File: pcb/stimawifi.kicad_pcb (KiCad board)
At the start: 2 copper layers, 62.9 x 48.8 mm, 12 parts, among them J1 Screw_Terminal_01x05, J2 Screw_Terminal_01x05, J3 Screw_Terminal_01x05, J4 Screw_Terminal_01x05, J5 Screw_Terminal_01x05, J8 Conn_01x02, U1 WEMOS_D1_mini

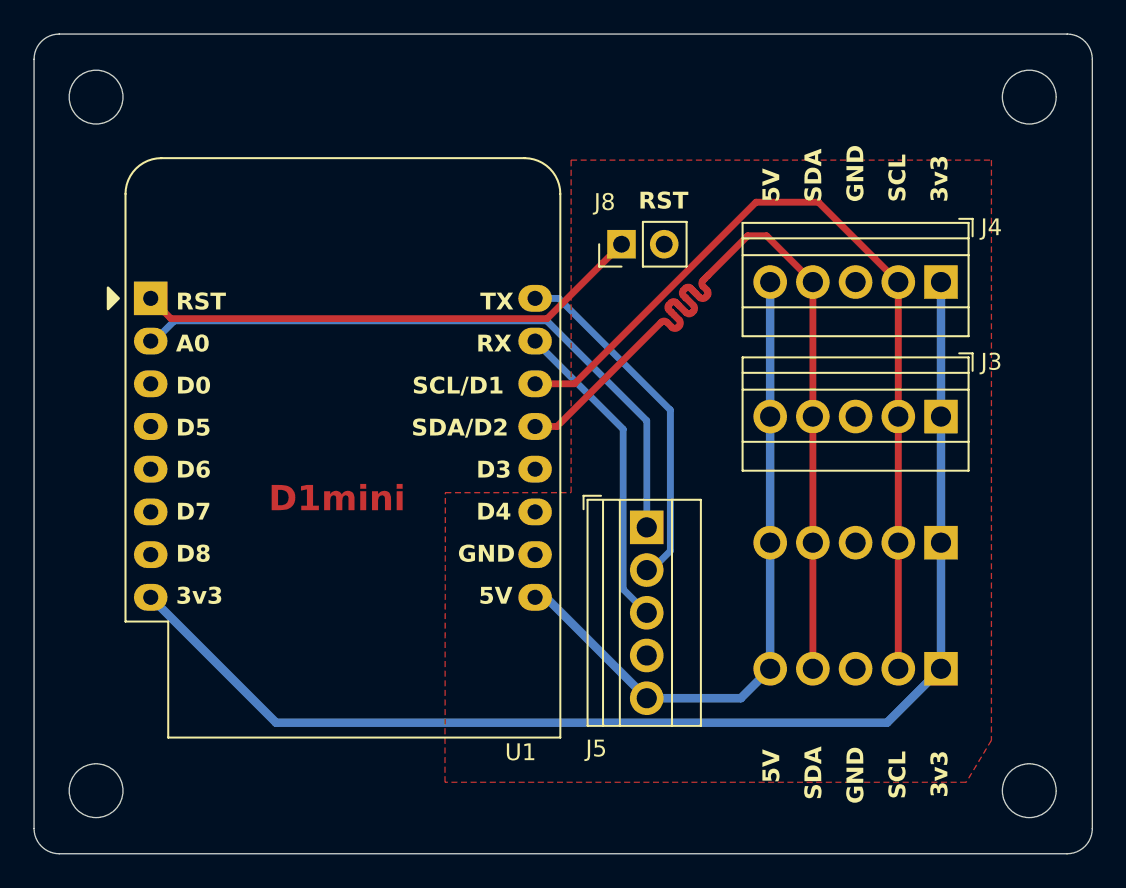
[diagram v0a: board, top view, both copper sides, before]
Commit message: Migrated symbols, footprint and 3d models to local libraries
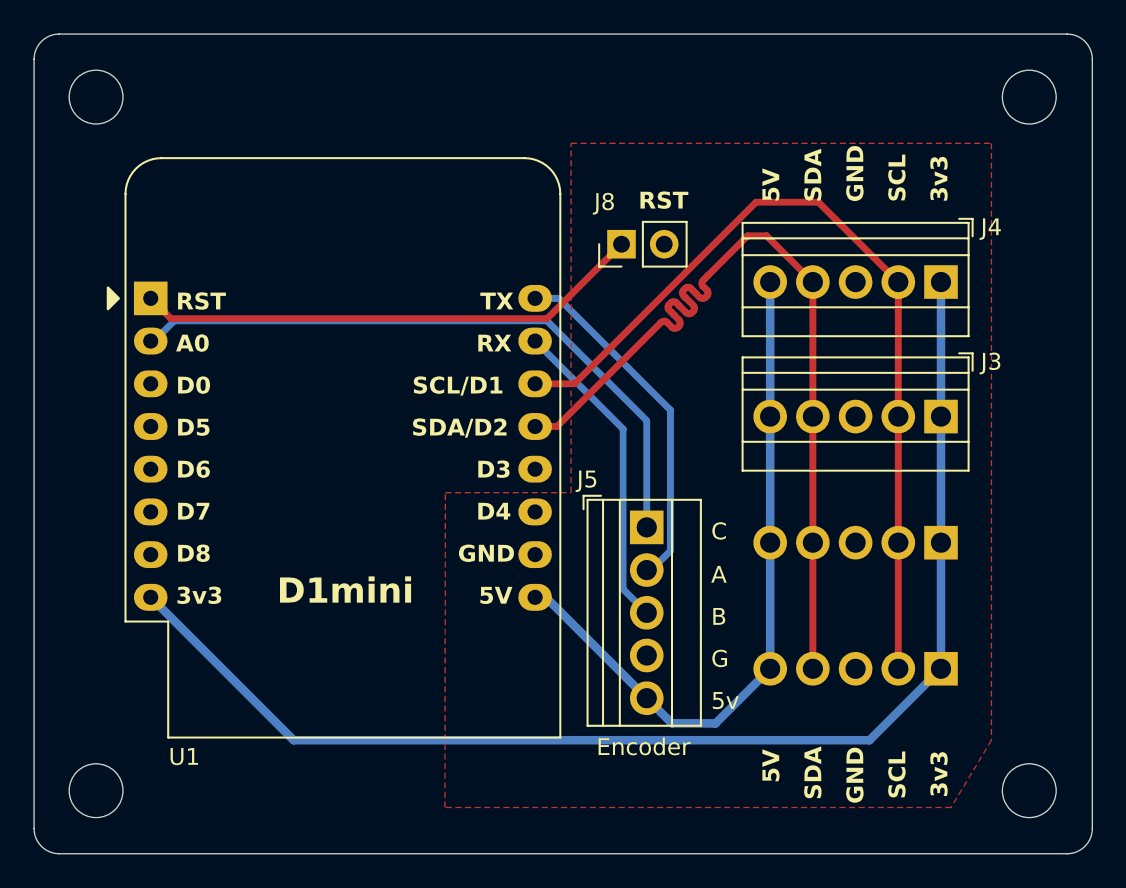
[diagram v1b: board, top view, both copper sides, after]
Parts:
- moved Open Hardvare Logo 1.00 mm to (164.0, 71.0)
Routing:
- net 5v: track 40.2 -> 41.4 mm
- net 3v3: track 74.4 -> 75.3 mm
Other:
- board text added: "5v"
- board text added: "A"
- board text added: "B"
- board text added: "C"
- board text added: "Encoder"
- board text added: "G"
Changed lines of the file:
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@@
 		(tags "THT Terminal Block Xinya XY308-2.54-5P pitch 2.54mm size 13.2x6.5mm^2 drill 1.2mm pad 2mm")
 		(property "Reference" "J5"
-			(at 13.16 3 180)
+			(at -2.84 3.52 0)
 			(layer "F.SilkS")
 			(effects
@@
 		)
 		(embedded_fonts no)
-		(model "${KICAD9_3DMODEL_DIR}/TerminalBlock_Phoenix.3dshapes/TerminalBlock_Phoenix_MPT-0,5-5-2.54_1x05_P2.54mm_Horizontal.step"
+		(model "${KIPRJMOD}/3d_models/TerminalBlock_Phoenix_MPT-0,5-5-2.54_1x05_P2.54mm_Horizontal.step"
 			(offset
 				(xyz 10.125 -0.125 0)
@@
 		(tags "ESP8266 WiFi microcontroller")
 		(property "Reference" "U1"
-			(at 22 27 0)
+			(at 2 27.28 0)
 			(layer "F.SilkS")
 			(effects
@@
 		)
 		(embedded_fonts no)
-		(model "${KICAD8_3DMODEL_DIR}/RF_Module.3dshapes/WEMOS_D1_mini_light.wrl"
+		(model "${KIPRJMOD}/3d_models/WEMOS_D1_mini_light.step"
 			(offset
 				(xyz 0 0 -0.5)
@@
 			)
 		)
-		(model "${KICAD9_3DMODEL_DIR}/Connector_PinSocket_2.54mm.3dshapes/PinSocket_1x08_P2.54mm_Vertical.step"
+		(model "${KIPRJMOD}/3d_models/PinSocket_1x08_P2.54mm_Vertical.step"
 			(offset
 				(xyz 0 0 0)
@@
 			)
 		)
-		(model "${KICAD9_3DMODEL_DIR}/Connector_PinSocket_2.54mm.3dshapes/PinSocket_1x08_P2.54mm_Vertical.step"
+		(model "${KIPRJMOD}/3d_models/PinSocket_1x08_P2.54mm_Vertical.step"
 			(offset
 				(xyz 23 0 0)
@@
 			)
 		)
-		(model "${KICAD9_3DMODEL_DIR}/Connector_PinSocket_2.54mm.3dshapes/PinSocket_1x08_P2.54mm_Vertical.step"
+		(model "${KIPRJMOD}/3d_models/PinSocket_1x08_P2.54mm_Vertical.step"
 			(offset
 				(xyz 0 0 10.5)
@@
 			)
 		)
-		(model "${KICAD9_3DMODEL_DIR}/Connector_PinSocket_2.54mm.3dshapes/PinSocket_1x08_P2.54mm_Vertical.step"
+		(model "${KIPRJMOD}/3d_models/PinSocket_1x08_P2.54mm_Vertical.step"
 			(offset
 				(xyz 23 0 10.5)
@@
 		)
 		(embedded_fonts no)
-		(model "${KICAD9_3DMODEL_DIR}/TerminalBlock_Phoenix.3dshapes/TerminalBlock_Phoenix_MPT-0,5-5-2.54_1x05_P2.54mm_Horizontal.step"
+		(model "${KIPRJMOD}/3d_models/TerminalBlock_Phoenix_MPT-0,5-5-2.54_1x05_P2.54mm_Horizontal.step"
 			(offset
 				(xyz 0 0 0)
@@
 		)
 		(embedded_fonts no)
-		(model "${KICAD8_3DMODEL_DIR}/Connector_PinHeader_2.54mm.3dshapes/PinHeader_1x02_P2.54mm_Vertical.wrl"
+		(model "${KIPRJMOD}/3d_models/PinHeader_1x02_P2.54mm_Vertical.step"
 			(offset
 				(xyz 0 0 0)
@@
 		)
 		(embedded_fonts no)
-		(model "${KICAD9_3DMODEL_DIR}/TerminalBlock_Phoenix.3dshapes/TerminalBlock_Phoenix_MPT-0,5-5-2.54_1x05_P2.54mm_Horizontal.step"
+		(model "${KIPRJMOD}/3d_models/TerminalBlock_Phoenix_MPT-0,5-5-2.54_1x05_P2.54mm_Horizontal.step"
 			(offset
 				(xyz 10.125 -0.175 0)
@@
 	(footprint "Stima.Library:ohlogo"
 		(layer "B.Cu")
-		(at 164 72 180)
+		(at 164 71 180)
 		(property "Reference" "Open Hardvare Logo"
 			(at 0 -7.5 0)
@@
 		)
 		(embedded_fonts no)
-		(model "${KICAD9_3DMODEL_DIR}/TerminalBlock_Phoenix.3dshapes/TerminalBlock_Phoenix_MPT-0,5-5-2.54_1x05_P2.54mm_Horizontal.step"
+		(model "${KIPRJMOD}/3d_models/TerminalBlock_Phoenix_MPT-0,5-5-2.54_1x05_P2.54mm_Horizontal.step"
 			(offset
 				(xyz 0 0 0)
@@
 		)
 		(embedded_fonts no)
-		(model "${KICAD9_3DMODEL_DIR}/TerminalBlock_Phoenix.3dshapes/TerminalBlock_Phoenix_MPT-0,5-5-2.54_1x05_P2.54mm_Horizontal.step"
+		(model "${KIPRJMOD}/3d_models/TerminalBlock_Phoenix_MPT-0,5-5-2.54_1x05_P2.54mm_Horizontal.step"
 			(offset
 				(xyz 10.125 -0.125 0)
@@
 		(layer "Edge.Cuts")
 	)
-	(gr_text "D1mini"
-		(at 159.5 74 0)
-		(layer "F.Cu")
-		(effects
-			(font
-				(size 1.5 1.5)
-				(thickness 0.3)
-				(bold yes)
-			)
-			(justify left bottom)
-		)
-	)
 	(gr_text "D3"
 		(at 171.857143 72 0)
@@
 		)
 	)
+	(gr_text "A"
+		(at 185.823953 78.254976 0)
+		(layer "F.SilkS")
+		(effects
+			(font
+				(size 1 1)
+				(thickness 0.1)
+			)
+			(justify left bottom)
+		)
+	)
+	(gr_text "Encoder"
+		(at 179 88.5 0)
+		(layer "F.SilkS")
+		(effects
+			(font
+				(size 1 1)
+				(thickness 0.1)
+			)
+			(justify left bottom)
+		)
+	)
 	(gr_text "3v3"
 		(at 200 90.904762 90)
@@
 		)
 	)
+	(gr_text "D1mini"
+		(at 160 79.5 0)
+		(layer "F.SilkS")
+		(effects
+			(font
+				(size 1.5 1.5)
+				(thickness 0.3)
+				(bold yes)
+			)
+			(justify left bottom)
+		)
+	)
 	(gr_text "SDA"
 		(at 192.5 91.047619 90)
@@
 		)
 	)
+	(gr_text "B"
+		(at 185.823953 80.754976 0)
+		(layer "F.SilkS")
+		(effects
+			(font
+				(size 1 1)
+				(thickness 0.1)
+			)
+			(justify left bottom)
+		)
+	)
+	(gr_text "C"
+		(at 185.823953 75.673469 0)
+		(layer "F.SilkS")
+		(effects
+			(font
+				(size 1 1)
+				(thickness 0.1)
+			)
+			(justify left bottom)
+		)
+	)
 	(gr_text "RX"
 		(at 171.857143 64.5 0)
@@
 		)
 	)
+	(gr_text "5v"
+		(at 185.823953 85.754976 0)
+		(layer "F.SilkS")
+		(effects
+			(font
+				(size 1 1)
+				(thickness 0.1)
+			)
+			(justify left bottom)
+		)
+	)
 	(gr_text "5V"
 		(at 190 55.5 90)
@@
 		)
 	)
+	(gr_text "G"
+		(at 185.823953 83.254976 0)
+		(layer "F.SilkS")
+		(effects
+			(font
+				(size 1 1)
+				(thickness 0.125)
+			)
+			(justify left bottom)
+		)
+	)
 	(gr_text "5V"
 		(at 190 88 90)
@@
 	)
 	(segment
-		(start 152.5 79)
-		(end 159.955 86.455)
-		(width 0.508)
-		(layer "B.Cu")
-		(net 1)
-	)
-	(segment
 		(start 199.5 83.25)
 		(end 199.5 75.75)
@@
 	)
 	(segment
-		(start 159.955 86.455)
-		(end 196.295 86.455)
+		(start 195.25 87.5)
+		(end 199.5 83.25)
 		(width 0.508)
 		(layer "B.Cu")
@@
 	)
 	(segment
-		(start 196.295 86.455)
-		(end 199.5 83.25)
+		(start 152.5 79)
+		(end 161 87.5)
 		(width 0.508)
 		(layer "B.Cu")
@@
 	)
 	(segment
+		(start 161 87.5)
+		(end 195.25 87.5)
+		(width 0.508)
+		(layer "B.Cu")
+		(net 1)
+	)
+	(segment
 		(start 185.43101 60.068989)
 		(end 185.633864 59.866136)
@@
 	)
 	(segment
-		(start 182 85)
-		(end 187.59 85)
+		(start 175.36 79)
+		(end 176 79)
 		(width 0.508)
 		(layer "B.Cu")
@@
 	)
 	(segment
-		(start 175.36 79)
-		(end 176 79)
+		(start 182 85)
+		(end 183.5 86.5)
 		(width 0.508)
 		(layer "B.Cu")
@@
 	)
 	(segment
-		(start 187.59 85)
+		(start 186.09 86.5)
 		(end 189.34 83.25)
 		(width 0.508)
@@
 	)
 	(segment
+		(start 183.5 86.5)
+		(end 186.09 86.5)
+		(width 0.508)
+		(layer "B.Cu")
+		(net 5)
+	)
+	(segment
 		(start 183.4042 76.2442)
 		(end 182.2684 77.38)
@@
 		(polygon
 			(pts
-				(xy 170 90) (xy 170.023618 72.773861) (xy 177.5 72.773443) (xy 177.5 53) (xy 202.5 53) (xy 202.5 87.5)
-				(xy 201 90)
+				(xy 169.997943 91.5) (xy 170.023618 72.773861) (xy 177.5 72.773443) (xy 177.5 52) (xy 202.5 52)
+				(xy 202.5 87.5) (xy 200.1 91.5)
 			)
 		)
